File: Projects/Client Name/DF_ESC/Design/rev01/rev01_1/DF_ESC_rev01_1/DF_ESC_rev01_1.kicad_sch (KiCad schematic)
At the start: 0 parts

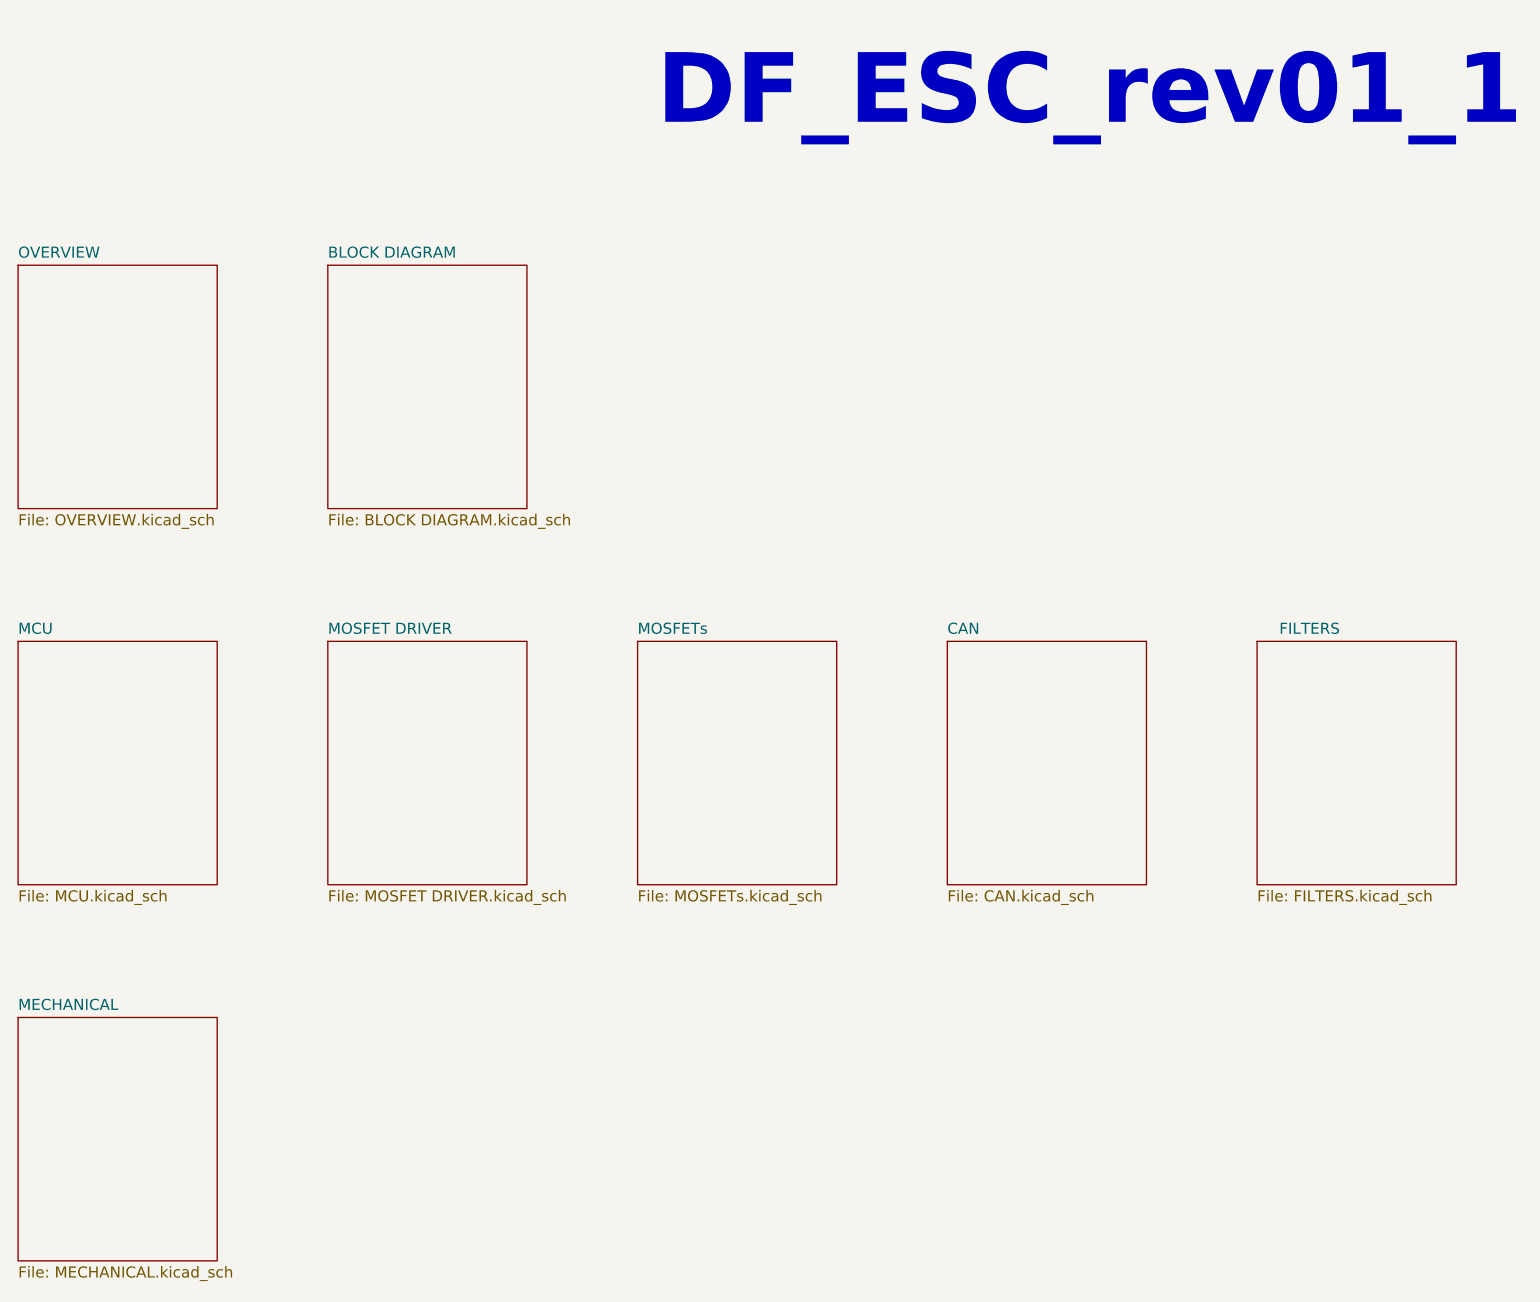
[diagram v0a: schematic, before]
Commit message: Update 19-01-2024 primera
cambiar y añadir numeracion de sheets
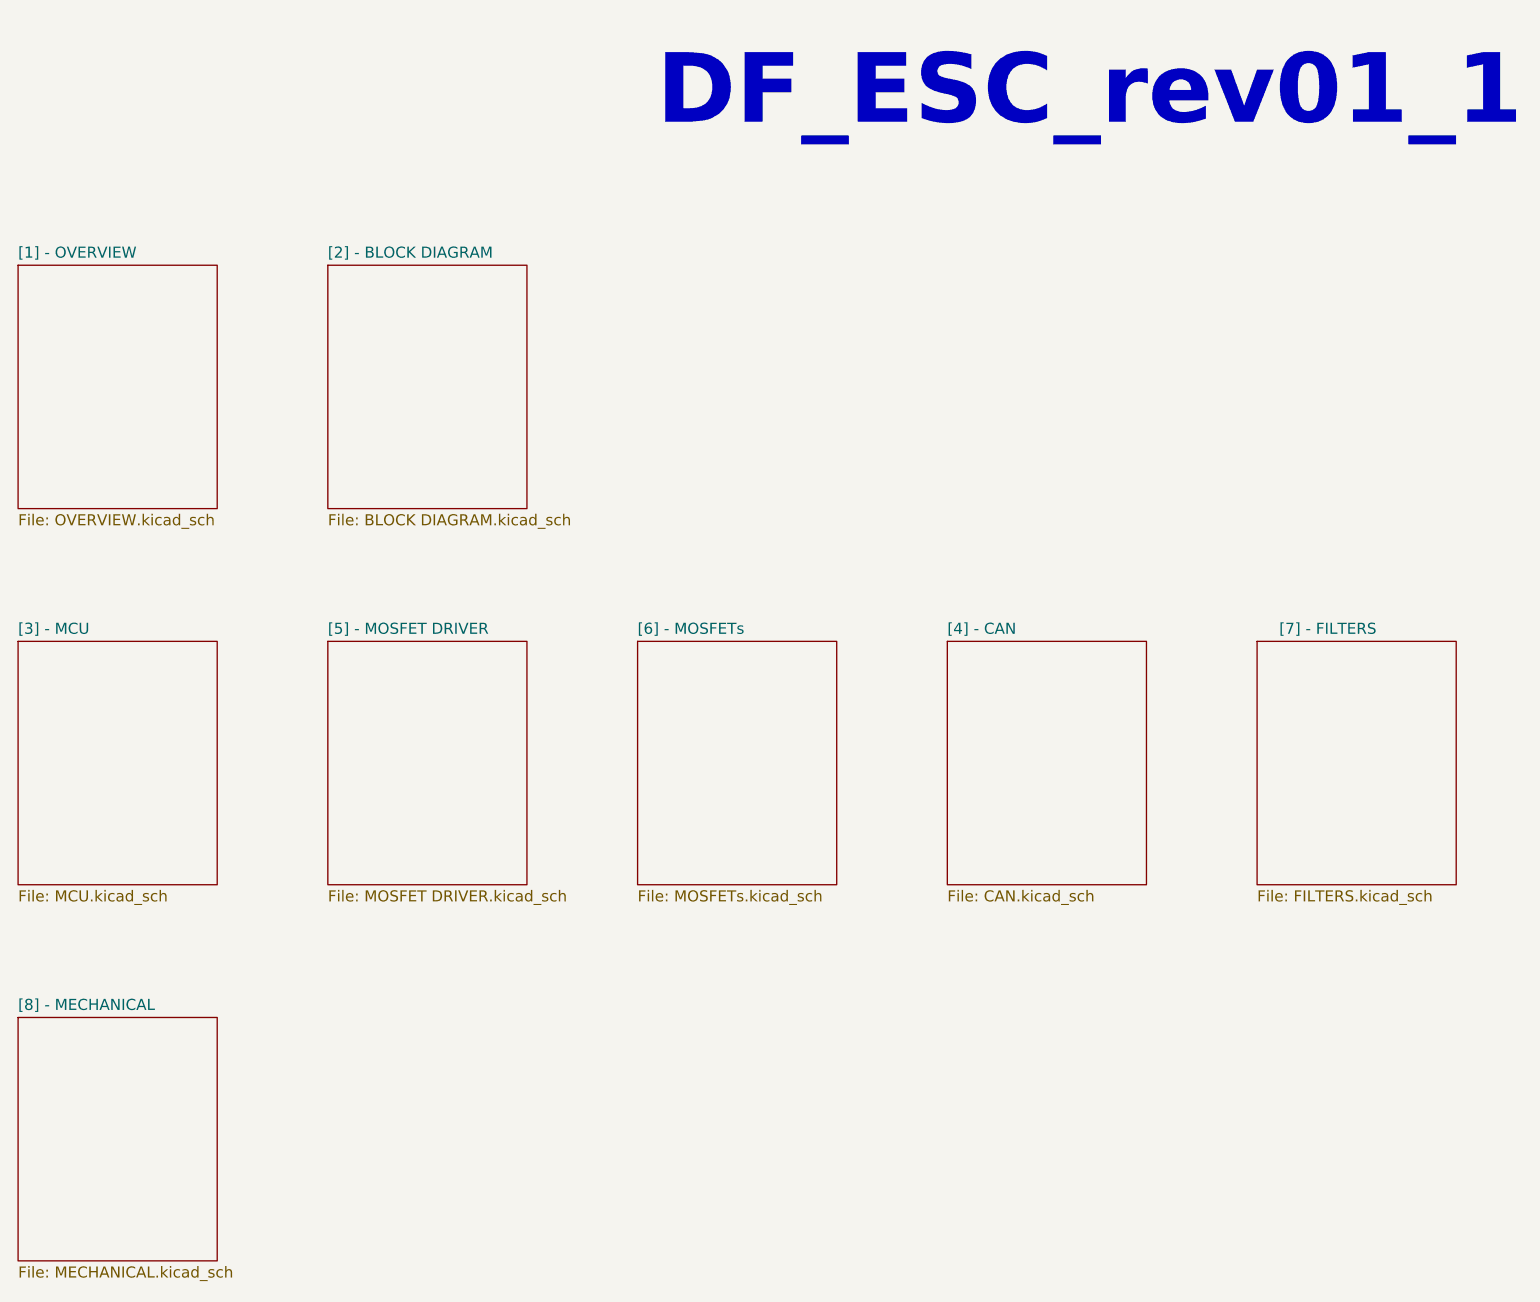
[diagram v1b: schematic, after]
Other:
- sheet BLOCK DIAGRAM renamed [2] - BLOCK DIAGRAM
- sheet CAN renamed [4] - CAN
- sheet FILTERS renamed [7] - FILTERS
- sheet MCU renamed [3] - MCU
- sheet MECHANICAL renamed [8] - MECHANICAL
- sheet MOSFET DRIVER renamed [5] - MOSFET DRIVER
- sheet MOSFETs renamed [6] - MOSFETs
- sheet OVERVIEW renamed [1] - OVERVIEW
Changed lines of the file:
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@@
     (stroke (width 0.1524) (type solid))
     (fill (color 0 0 0 0.0000))
-    (property "Sheetname" "MCU" (at 35.56 84.3784 0)
+    (property "Sheetname" "[3] - MCU" (at 35.56 84.3784 0)
       (effects (font (size 1.27 1.27)) (justify left bottom))
     )
@@
     (instances
       (project "DF_ESC_rev01_1"
-        (path "/e63e39d7-6ac0-4ffd-8aa3-1841a4541b55" (page "5"))
+        (path "/e63e39d7-6ac0-4ffd-8aa3-1841a4541b55" (page "4"))
       )
     )
@@
     (stroke (width 0.1524) (type solid))
     (fill (color 0 0 0 0.0000))
-    (property "Sheetname" "FILTERS" (at 180.34 84.3784 0)
+    (property "Sheetname" "[7] - FILTERS" (at 180.34 84.3784 0)
       (effects (font (size 1.27 1.27)) (justify left bottom))
     )
@@
     (stroke (width 0.1524) (type solid))
     (fill (color 0 0 0 0.0000))
-    (property "Sheetname" "BLOCK DIAGRAM" (at 71.12 41.1984 0)
+    (property "Sheetname" "[2] - BLOCK DIAGRAM" (at 71.12 41.1984 0)
       (effects (font (size 1.27 1.27)) (justify left bottom))
     )
@@
     (stroke (width 0.1524) (type solid))
     (fill (color 0 0 0 0.0000))
-    (property "Sheetname" "MOSFETs" (at 106.68 84.3784 0)
+    (property "Sheetname" "[6] - MOSFETs" (at 106.68 84.3784 0)
       (effects (font (size 1.27 1.27)) (justify left bottom))
     )
@@
     (stroke (width 0.1524) (type solid))
     (fill (color 0 0 0 0.0000))
-    (property "Sheetname" "CAN" (at 142.24 84.3784 0)
+    (property "Sheetname" "[4] - CAN" (at 142.24 84.3784 0)
       (effects (font (size 1.27 1.27)) (justify left bottom))
     )
@@
     (instances
       (project "DF_ESC_rev01_1"
-        (path "/e63e39d7-6ac0-4ffd-8aa3-1841a4541b55" (page "4"))
+        (path "/e63e39d7-6ac0-4ffd-8aa3-1841a4541b55" (page "5"))
       )
     )
@@
     (stroke (width 0.1524) (type solid))
     (fill (color 0 0 0 0.0000))
-    (property "Sheetname" "MECHANICAL" (at 35.56 127.5584 0)
+    (property "Sheetname" "[8] - MECHANICAL" (at 35.56 127.5584 0)
       (effects (font (size 1.27 1.27)) (justify left bottom))
     )
@@
     (stroke (width 0.1524) (type solid))
     (fill (color 0 0 0 0.0000))
-    (property "Sheetname" "OVERVIEW" (at 35.56 41.1984 0)
+    (property "Sheetname" "[1] - OVERVIEW" (at 35.56 41.1984 0)
       (effects (font (size 1.27 1.27)) (justify left bottom))
     )
@@
     (stroke (width 0.1524) (type solid))
     (fill (color 0 0 0 0.0000))
-    (property "Sheetname" "MOSFET DRIVER" (at 71.12 84.3784 0)
+    (property "Sheetname" "[5] - MOSFET DRIVER" (at 71.12 84.3784 0)
       (effects (font (size 1.27 1.27)) (justify left bottom))
     )
